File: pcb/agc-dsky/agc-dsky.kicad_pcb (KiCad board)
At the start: 2 copper layers, 100 x 100 mm, 130 parts, among them IC1 TPS62132, IC10 LDS-3161AX, IC11 LDS-3161AX, IC12 LDS-3161AX, IC13 LDS-3161AX, IC14 LDS-3161AX, IC15 LDS-3161AX, IC16 LDS-3161AX, IC17 LDS-3161AX, IC18 LDS-3161AX, IC19 LDS-3161AX, IC2 STM32F072RBT6, IC20 LDS-3161AX, IC21 LDS-3161AX, IC22 LDS-3161AX, IC23 LDS-3161AX, IC24 LDS-3161AX, IC25 LDS-3161AX, IC26 LDS-3161AX, IC27 LDS-3161AX, IC3 MCP23S08, IC4 MCP23S08, IC5 MCP23S08, IC6 MCP23S08, IC7 LDS-3161AX, IC8 LDS-3161AX, IC9 LDS-3161AX, J1 MICROUSB, P1 SWD_TC, Q1 FDN327N, Q2 FDN327N, Q3 FDN327N, Q4 FDN327N, Q5 FDN327N, Q6 FDN327N, SW1 SKPMAME010, SW10 SKPMAME010, SW11 SKPMAME010, SW12 SKPMAME010, SW13 SKPMAME010, SW14 SKPMAME010, SW15 SKPMAME010, SW16 SKPMAME010, SW17 SKPMAME010, SW18 SKPMAME010, SW19 SKPMAME010, SW2 SKPMAME010, SW20 SKPMAME010, SW3 SKPMAME010, SW4 SKPMAME010, SW5 SKPMAME010, SW6 SKPMAME010, SW7 SKPMAME010, SW8 SKPMAME010, SW9 SKHHALA010

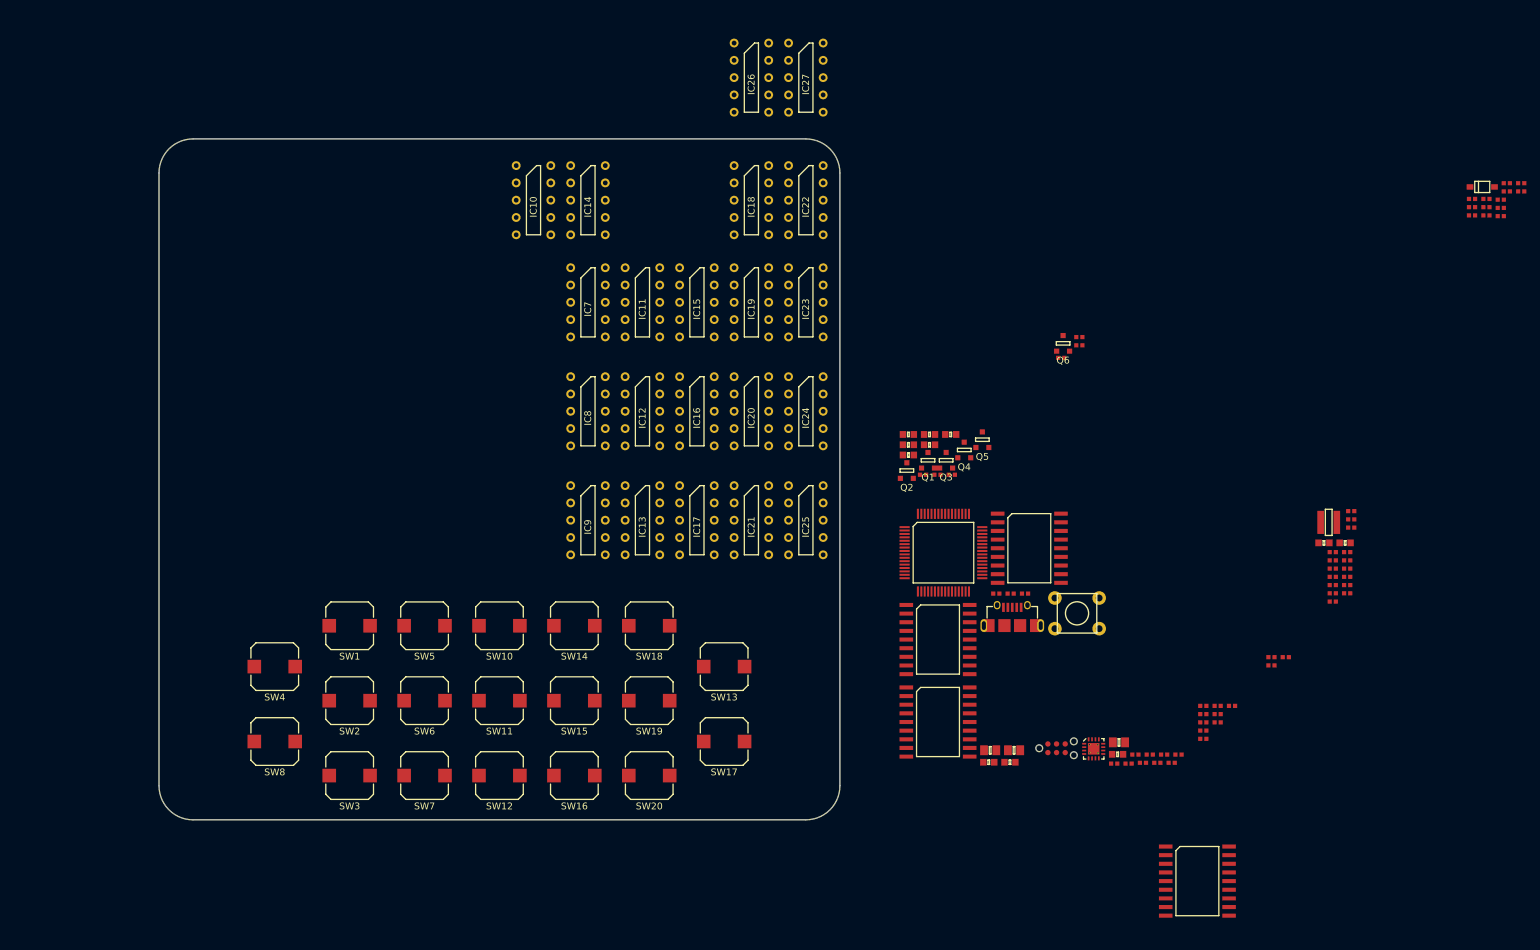
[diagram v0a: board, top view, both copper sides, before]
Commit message: Progress with DSKY board layout
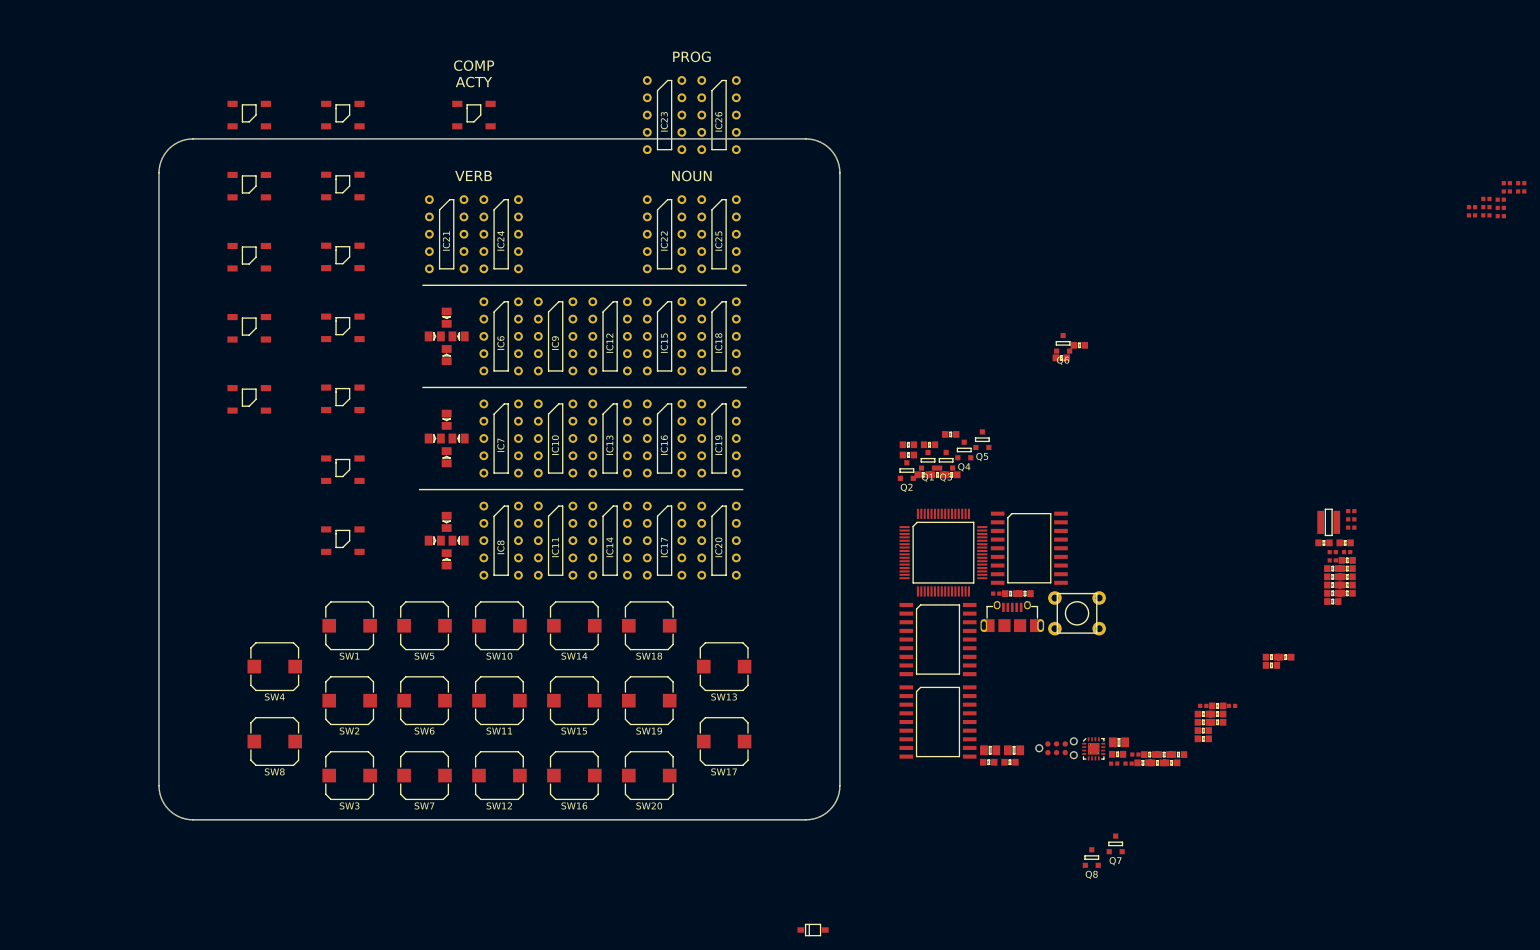
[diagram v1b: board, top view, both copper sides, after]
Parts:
- removed C31: 100nF, agg:0402
- removed R40, R42: 1M, agg:0603
- removed R41: 120, agg:0402
- added D10: LED, agg:0805-LED, F.Cu at (120.5, 74.0)
- added D11: LED, agg:0805-LED, F.Cu at (120.5, 89.0)
- added D12: LED, agg:0805-LED, F.Cu at (120.5, 104.0)
- added D13: MMSD4148T1G, agg:SOD-123, F.Cu at (176.1, 161.2)
- added D2: LED, agg:0805-LED, F.Cu at (122.2, 86.2)
- added D3: LED, agg:0805-LED, F.Cu at (122.2, 101.2)
- added D4: LED, agg:0805-LED, F.Cu at (124.0, 74.0)
- added D5: LED, agg:0805-LED, F.Cu at (124.0, 89.0)
- added D6: LED, agg:0805-LED, F.Cu at (124.0, 104.0)
- added D7: LED, agg:0805-LED, F.Cu at (122.2, 76.8)
- added D8: LED, agg:0805-LED, F.Cu at (122.2, 91.8)
- added D9: LED, agg:0805-LED, F.Cu at (122.2, 106.8)
- added IC28: WS2812B, agc-dsky:WS2812B, F.Cu at (93.2, 41.5)
- added IC29: WS2812B, agc-dsky:WS2812B, F.Cu at (93.2, 51.9)
- added IC30: WS2812B, agc-dsky:WS2812B, F.Cu at (93.2, 62.4)
- added IC31: WS2812B, agc-dsky:WS2812B, F.Cu at (93.2, 72.8)
- added IC32: WS2812B, agc-dsky:WS2812B, F.Cu at (93.2, 83.2)
- added IC33: WS2812B, agc-dsky:WS2812B, F.Cu at (107.0, 41.5)
- added IC34: WS2812B, agc-dsky:WS2812B, F.Cu at (107.0, 51.9)
- added IC35: WS2812B, agc-dsky:WS2812B, F.Cu at (107.0, 62.3)
- added IC36: WS2812B, agc-dsky:WS2812B, F.Cu at (107.0, 72.7)
- added IC37: WS2812B, agc-dsky:WS2812B, F.Cu at (107.0, 83.2)
- added IC38: WS2812B, agc-dsky:WS2812B, F.Cu at (107.0, 93.6)
- added IC39: WS2812B, agc-dsky:WS2812B, F.Cu at (107.0, 104.0)
- added Q7: FDN327N, agc-dsky:supersot-3, F.Cu at (220.5, 148.5)
- added Q8: FDN327N, agc-dsky:supersot-3, F.Cu at (217.0, 150.5)
- D1: value MMSD4148T1G -> LED; footprint agg:SOD-123 -> agg:0805-LED
- IC27: value LDS-3161AX -> WS2812B; footprint agc-dsky:LDS-3161AX -> agc-dsky:WS2812B
- IC6: value MCP23S08 -> LDS-3161AX; footprint agc-dsky:SOIC-18-W -> agc-dsky:LDS-3161AX
- R10, R11, R12, R13, R14, R15, R16, R17, R18, R19, R20, R21, R22, R23, R24, R26, R28, R3, R30, R4, R5, R6, R7, R8, R9: value 120 -> 100; footprint agg:0402 -> agg:0603
- R25, R27, R29, R31, R33, R35, R37, R39: value 120 -> 1M; footprint agg:0402 -> agg:0603
- R32, R34, R36, R38: value 1M -> 100
- moved D1 153.3 mm to (122.2, 71.2), turned to 90 degrees
- moved IC6 129.8 mm to (130.2, 74.0)
- moved IC21 61.4 mm to (122.2, 59.0)
- moved IC24 51.8 mm to (130.2, 59.0)
- moved IC14 50.1 mm to (146.2, 104.0)
- moved IC27 49.1 mm to (126.2, 41.5)
- moved IC25 43.9 mm to (162.2, 59.0)
- moved IC11 37.2 mm to (138.2, 104.0)
- moved IC10 35.2 mm to (138.2, 89.0)
- moved IC23 34.5 mm to (154.2, 41.5)
- moved IC9 27.4 mm to (138.2, 74.0)
- moved IC7 23.7 mm to (130.2, 89.0)
- moved IC8 22.9 mm to (130.2, 104.0)
- moved IC22 21.3 mm to (154.2, 59.0)
- moved IC18 20.6 mm to (162.2, 74.0)
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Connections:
- C18 pad 1: 3v3 -> 5v
- C19 pad 1: Net-(C19-Pad1) -> 5v
- C23 pad 1: 5v -> Net-(C23-Pad1)
- D1 pad 1: Net-(C19-Pad1) -> Net-(D1-Pad1)
- D1 pad 2: 5v -> /7-segs/D1
- IC10 pad 10: /7-segs/A4 -> /7-segs/A2
- IC10 pad 2: /7-segs/F4 -> /7-segs/F2
- IC10 pad 3: /7-segs/G4 -> /7-segs/G2
- IC10 pad 4: /7-segs/E4 -> /7-segs/E2
- IC10 pad 5: /7-segs/D4 -> /7-segs/D2
- IC10 pad 8: /7-segs/C4 -> /7-segs/C2
- IC10 pad 9: /7-segs/B4 -> /7-segs/B2
- IC11 pad 1: Net-(IC11-Pad1) -> Net-(IC10-Pad1)
- IC11 pad 10: /7-segs/A1 -> /7-segs/A3
- IC11 pad 2: /7-segs/F1 -> /7-segs/F3
- IC11 pad 3: /7-segs/G1 -> /7-segs/G3
- IC11 pad 4: /7-segs/E1 -> /7-segs/E3
- IC11 pad 5: /7-segs/D1 -> /7-segs/D3
- IC11 pad 6: Net-(IC11-Pad1) -> Net-(IC10-Pad1)
- IC11 pad 8: /7-segs/C1 -> /7-segs/C3
- IC11 pad 9: /7-segs/B1 -> /7-segs/B3
- IC12 pad 1: Net-(IC11-Pad1) -> Net-(IC12-Pad1)
- IC12 pad 10: /7-segs/A2 -> /7-segs/A1
- IC12 pad 2: /7-segs/F2 -> /7-segs/F1
- IC12 pad 3: /7-segs/G2 -> /7-segs/G1
- IC12 pad 4: /7-segs/E2 -> /7-segs/E1
- IC12 pad 5: /7-segs/D2 -> /7-segs/D1
- IC12 pad 6: Net-(IC11-Pad1) -> Net-(IC12-Pad1)
- IC12 pad 8: /7-segs/C2 -> /7-segs/C1
- IC12 pad 9: /7-segs/B2 -> /7-segs/B1
- IC13 pad 1: Net-(IC11-Pad1) -> Net-(IC12-Pad1)
- IC13 pad 10: /7-segs/A3 -> /7-segs/A2
- IC13 pad 2: /7-segs/F3 -> /7-segs/F2
- IC13 pad 3: /7-segs/G3 -> /7-segs/G2
- IC13 pad 4: /7-segs/E3 -> /7-segs/E2
- IC13 pad 5: /7-segs/D3 -> /7-segs/D2
- IC13 pad 6: Net-(IC11-Pad1) -> Net-(IC12-Pad1)
- IC13 pad 8: /7-segs/C3 -> /7-segs/C2
- IC13 pad 9: /7-segs/B3 -> /7-segs/B2
- IC14 pad 1: Net-(IC11-Pad1) -> Net-(IC12-Pad1)
- IC14 pad 10: /7-segs/A4 -> /7-segs/A3
- IC14 pad 2: /7-segs/F4 -> /7-segs/F3
- IC14 pad 3: /7-segs/G4 -> /7-segs/G3
- IC14 pad 4: /7-segs/E4 -> /7-segs/E3
- IC14 pad 5: /7-segs/D4 -> /7-segs/D3
- IC14 pad 6: Net-(IC11-Pad1) -> Net-(IC12-Pad1)
- IC14 pad 8: /7-segs/C4 -> /7-segs/C3
- IC14 pad 9: /7-segs/B4 -> /7-segs/B3
- IC18 pad 1: Net-(IC15-Pad1) -> Net-(IC18-Pad1)
- IC18 pad 10: /7-segs/A4 -> /7-segs/A1
- IC18 pad 2: /7-segs/F4 -> /7-segs/F1
- IC18 pad 3: /7-segs/G4 -> /7-segs/G1
- IC18 pad 4: /7-segs/E4 -> /7-segs/E1
- IC18 pad 5: /7-segs/D4 -> /7-segs/D1
- IC18 pad 6: Net-(IC15-Pad1) -> Net-(IC18-Pad1)
- IC18 pad 8: /7-segs/C4 -> /7-segs/C1
- IC18 pad 9: /7-segs/B4 -> /7-segs/B1
- IC19 pad 1: Net-(IC19-Pad1) -> Net-(IC18-Pad1)
- IC19 pad 10: /7-segs/A1 -> /7-segs/A2
- IC19 pad 2: /7-segs/F1 -> /7-segs/F2
- IC19 pad 3: /7-segs/G1 -> /7-segs/G2
- IC19 pad 4: /7-segs/E1 -> /7-segs/E2
- IC19 pad 5: /7-segs/D1 -> /7-segs/D2
- IC19 pad 6: Net-(IC19-Pad1) -> Net-(IC18-Pad1)
- IC19 pad 8: /7-segs/C1 -> /7-segs/C2
- IC19 pad 9: /7-segs/B1 -> /7-segs/B2
- IC2 pad 10: Net-(IC2-Pad10) -> (no net)
- IC2 pad 11: Net-(IC2-Pad11) -> (no net)
- IC2 pad 14: Net-(IC2-Pad14) -> (no net)
- IC2 pad 15: Net-(IC2-Pad15) -> (no net)
- IC2 pad 16: Net-(IC2-Pad16) -> (no net)
- IC2 pad 17: Net-(IC2-Pad17) -> (no net)
- IC2 pad 20: Net-(IC2-Pad20) -> (no net)
- IC2 pad 28: Net-(IC2-Pad28) -> (no net)
- IC2 pad 29: Net-(IC2-Pad29) -> /Co8
- IC2 pad 3: Net-(IC2-Pad3) -> (no net)
- IC2 pad 37: /NRST_4 -> (no net)
- IC2 pad 38: /NCS_4 -> (no net)
- IC2 pad 4: Net-(IC2-Pad4) -> (no net)
- IC2 pad 5: Net-(IC2-Pad5) -> (no net)
- IC2 pad 50: Net-(IC2-Pad50) -> (no net)
- IC2 pad 51: Net-(IC2-Pad51) -> (no net)
- IC2 pad 52: Net-(IC2-Pad52) -> (no net)
- IC2 pad 53: Net-(IC2-Pad53) -> (no net)
- IC2 pad 54: Net-(IC2-Pad54) -> (no net)
- IC2 pad 6: Net-(IC2-Pad6) -> (no net)
- IC2 pad 62: Net-(IC2-Pad62) -> /Co7
- IC2 pad 8: Net-(IC2-Pad8) -> (no net)
- IC2 pad 9: Net-(IC2-Pad9) -> (no net)
- IC20 pad 1: Net-(IC19-Pad1) -> Net-(IC18-Pad1)
- IC20 pad 10: /7-segs/A2 -> /7-segs/A3
- IC20 pad 2: /7-segs/F2 -> /7-segs/F3
- IC20 pad 3: /7-segs/G2 -> /7-segs/G3
- IC20 pad 4: /7-segs/E2 -> /7-segs/E3
- IC20 pad 5: /7-segs/D2 -> /7-segs/D3
- IC20 pad 6: Net-(IC19-Pad1) -> Net-(IC18-Pad1)
- IC20 pad 8: /7-segs/C2 -> /7-segs/C3
- IC20 pad 9: /7-segs/B2 -> /7-segs/B3
- IC21 pad 1: Net-(IC19-Pad1) -> Net-(IC21-Pad1)
- IC21 pad 10: /7-segs/A3 -> /7-segs/A1
- IC21 pad 2: /7-segs/F3 -> /7-segs/F1
- IC21 pad 3: /7-segs/G3 -> /7-segs/G1
- IC21 pad 4: /7-segs/E3 -> /7-segs/E1
- IC21 pad 5: /7-segs/D3 -> /7-segs/D1
- IC21 pad 6: Net-(IC19-Pad1) -> Net-(IC21-Pad1)
- IC21 pad 8: /7-segs/C3 -> /7-segs/C1
- IC21 pad 9: /7-segs/B3 -> /7-segs/B1
- IC22 pad 1: Net-(IC19-Pad1) -> Net-(IC21-Pad1)
- IC22 pad 10: /7-segs/A4 -> /7-segs/A2
- IC22 pad 2: /7-segs/F4 -> /7-segs/F2
- IC22 pad 3: /7-segs/G4 -> /7-segs/G2
- IC22 pad 4: /7-segs/E4 -> /7-segs/E2
- IC22 pad 5: /7-segs/D4 -> /7-segs/D2
- IC22 pad 6: Net-(IC19-Pad1) -> Net-(IC21-Pad1)
- IC22 pad 8: /7-segs/C4 -> /7-segs/C2
- IC22 pad 9: /7-segs/B4 -> /7-segs/B2
- IC23 pad 1: Net-(IC23-Pad1) -> Net-(IC21-Pad1)
- IC23 pad 10: /7-segs/A1 -> /7-segs/A3
- IC23 pad 2: /7-segs/F1 -> /7-segs/F3
- IC23 pad 3: /7-segs/G1 -> /7-segs/G3
- IC23 pad 4: /7-segs/E1 -> /7-segs/E3
- IC23 pad 5: /7-segs/D1 -> /7-segs/D3
- IC23 pad 6: Net-(IC23-Pad1) -> Net-(IC21-Pad1)
- IC23 pad 8: /7-segs/C1 -> /7-segs/C3
- IC23 pad 9: /7-segs/B1 -> /7-segs/B3
- IC24 pad 1: Net-(IC23-Pad1) -> Net-(IC24-Pad1)
- IC24 pad 10: /7-segs/A2 -> /7-segs/A1
- IC24 pad 2: /7-segs/F2 -> /7-segs/F1
- IC24 pad 3: /7-segs/G2 -> /7-segs/G1
- IC24 pad 4: /7-segs/E2 -> /7-segs/E1
- IC24 pad 5: /7-segs/D2 -> /7-segs/D1
- IC24 pad 6: Net-(IC23-Pad1) -> Net-(IC24-Pad1)
- IC24 pad 8: /7-segs/C2 -> /7-segs/C1
- IC24 pad 9: /7-segs/B2 -> /7-segs/B1
- IC25 pad 1: Net-(IC23-Pad1) -> Net-(IC24-Pad1)
- IC25 pad 10: /7-segs/A3 -> /7-segs/A2
- IC25 pad 2: /7-segs/F3 -> /7-segs/F2
- IC25 pad 3: /7-segs/G3 -> /7-segs/G2
- IC25 pad 4: /7-segs/E3 -> /7-segs/E2
- IC25 pad 5: /7-segs/D3 -> /7-segs/D2
- IC25 pad 6: Net-(IC23-Pad1) -> Net-(IC24-Pad1)
- IC25 pad 8: /7-segs/C3 -> /7-segs/C2
- IC25 pad 9: /7-segs/B3 -> /7-segs/B2
- IC26 pad 1: Net-(IC23-Pad1) -> Net-(IC24-Pad1)
- IC26 pad 10: /7-segs/A4 -> /7-segs/A3
- IC26 pad 2: /7-segs/F4 -> /7-segs/F3
- IC26 pad 3: /7-segs/G4 -> /7-segs/G3
- IC26 pad 4: /7-segs/E4 -> /7-segs/E3
- IC26 pad 5: /7-segs/D4 -> /7-segs/D3
- IC26 pad 6: Net-(IC23-Pad1) -> Net-(IC24-Pad1)
- IC26 pad 8: /7-segs/C4 -> /7-segs/C3
- IC26 pad 9: /7-segs/B4 -> /7-segs/B3
- IC27 pad 1: Net-(IC27-Pad1) -> Net-(C23-Pad1)
- IC27 pad 2: /7-segs/F4 -> Net-(IC27-Pad2)
- IC27 pad 3: /7-segs/G4 -> GND
- IC27 pad 4: /7-segs/E4 -> /LED_DIN
- IC3 pad 17: Net-(IC3-Pad17) -> (no net)
- IC3 pad 8: Net-(IC3-Pad8) -> (no net)
- IC4 pad 17: Net-(IC4-Pad17) -> (no net)
- IC4 pad 8: Net-(IC4-Pad8) -> (no net)
- IC5 pad 17: Net-(IC5-Pad17) -> (no net)
- IC5 pad 5: GND -> 3v3
- IC5 pad 8: Net-(IC5-Pad8) -> (no net)
- IC6 pad 1: /SPI2_SCK -> Net-(IC6-Pad1)
- IC6 pad 10: Net-(IC6-Pad10) -> /7-segs/A1
- IC6 pad 2: /SPI2_SI -> /7-segs/F1
- IC6 pad 3: /SPI2_SO -> /7-segs/G1
- IC6 pad 4: 3v3 -> /7-segs/E1
- IC6 pad 5: 3v3 -> /7-segs/D1
- IC6 pad 6: /NRST_4 -> Net-(IC6-Pad1)
- IC6 pad 7: /NCS_4 -> GND
- IC6 pad 8: Net-(IC6-Pad8) -> /7-segs/C1
- IC6 pad 9: GND -> /7-segs/B1
- IC7 pad 1: Net-(IC10-Pad1) -> Net-(IC6-Pad1)
- IC7 pad 10: /7-segs/A1 -> /7-segs/A2
- IC7 pad 2: /7-segs/F1 -> /7-segs/F2
- IC7 pad 3: /7-segs/G1 -> /7-segs/G2
- IC7 pad 4: /7-segs/E1 -> /7-segs/E2
- IC7 pad 5: /7-segs/D1 -> /7-segs/D2
- IC7 pad 6: Net-(IC10-Pad1) -> Net-(IC6-Pad1)
- IC7 pad 8: /7-segs/C1 -> /7-segs/C2
- IC7 pad 9: /7-segs/B1 -> /7-segs/B2
- IC8 pad 1: Net-(IC10-Pad1) -> Net-(IC6-Pad1)
- IC8 pad 10: /7-segs/A2 -> /7-segs/A3
- IC8 pad 2: /7-segs/F2 -> /7-segs/F3
- IC8 pad 3: /7-segs/G2 -> /7-segs/G3
- IC8 pad 4: /7-segs/E2 -> /7-segs/E3
- IC8 pad 5: /7-segs/D2 -> /7-segs/D3
- IC8 pad 6: Net-(IC10-Pad1) -> Net-(IC6-Pad1)
- IC8 pad 8: /7-segs/C2 -> /7-segs/C3
- IC8 pad 9: /7-segs/B2 -> /7-segs/B3
- IC9 pad 10: /7-segs/A3 -> /7-segs/A1
- IC9 pad 2: /7-segs/F3 -> /7-segs/F1
- IC9 pad 3: /7-segs/G3 -> /7-segs/G1
- IC9 pad 4: /7-segs/E3 -> /7-segs/E1
- IC9 pad 5: /7-segs/D3 -> /7-segs/D1
- IC9 pad 8: /7-segs/C3 -> /7-segs/C1
- IC9 pad 9: /7-segs/B3 -> /7-segs/B1
- J1 pad 4: Net-(J1-Pad4) -> (no net)
- J1 pad S: Net-(J1-PadS) -> (no net)
- P1 pad 6: Net-(P1-Pad6) -> (no net)
- Q1 pad D: Net-(IC10-Pad1) -> Net-(IC6-Pad1)
- Q2 pad D: Net-(IC11-Pad1) -> Net-(IC10-Pad1)
- Q3 pad D: Net-(IC15-Pad1) -> Net-(IC12-Pad1)
- Q4 pad D: Net-(IC19-Pad1) -> Net-(IC15-Pad1)
- Q5 pad D: Net-(IC23-Pad1) -> Net-(IC18-Pad1)
- Q6 pad D: Net-(IC27-Pad1) -> Net-(IC21-Pad1)
- R10 pad 1: /7-segs/F4 -> Net-(IC3-Pad14)
- R10 pad 2: Net-(IC6-Pad15) -> /7-segs/E1
- R11 pad 1: /7-segs/B1 -> Net-(IC4-Pad11)
- R11 pad 2: Net-(IC3-Pad11) -> /7-segs/B2
- R12 pad 1: /7-segs/E1 -> Net-(IC4-Pad14)
- R12 pad 2: Net-(IC3-Pad14) -> /7-segs/E2
- R13 pad 1: /7-segs/B2 -> Net-(IC5-Pad11)
- R13 pad 2: Net-(IC4-Pad11) -> /7-segs/B3
- R14 pad 1: /7-segs/E2 -> Net-(IC5-Pad14)
- R14 pad 2: Net-(IC4-Pad14) -> /7-segs/E3
- R15 pad 1: /7-segs/B3 -> Net-(IC3-Pad10)
- R15 pad 2: Net-(IC5-Pad11) -> /7-segs/A1
- R16 pad 1: /7-segs/E3 -> Net-(IC3-Pad13)
- R16 pad 2: Net-(IC5-Pad14) -> /7-segs/D1
- R17 pad 1: /7-segs/B4 -> Net-(IC3-Pad16)
- R17 pad 2: Net-(IC6-Pad11) -> /7-segs/G1
- R18 pad 1: /7-segs/E4 -> Net-(IC4-Pad10)
- R18 pad 2: Net-(IC6-Pad14) -> /7-segs/A2
- R19 pad 1: /7-segs/A1 -> Net-(IC4-Pad13)
- R19 pad 2: Net-(IC3-Pad10) -> /7-segs/D2
- R20 pad 1: /7-segs/D1 -> Net-(IC4-Pad16)
- R20 pad 2: Net-(IC3-Pad13) -> /7-segs/G2
- R21 pad 1: /7-segs/G1 -> Net-(IC5-Pad10)
- R21 pad 2: Net-(IC3-Pad16) -> /7-segs/A3
- R22 pad 1: /7-segs/A2 -> Net-(IC5-Pad13)
- R22 pad 2: Net-(IC4-Pad10) -> /7-segs/D3
- R23 pad 1: /7-segs/D2 -> Net-(IC5-Pad16)
- R23 pad 2: Net-(IC4-Pad13) -> /7-segs/G3
- R24 pad 1: /7-segs/G2 -> /Co1
- R24 pad 2: Net-(IC4-Pad16) -> Net-(Q1-PadG)
- R25 pad 1: /7-segs/A3 -> Net-(Q1-PadG)
- R25 pad 2: Net-(IC5-Pad10) -> GND
- R26 pad 1: /7-segs/D3 -> /Co2
- R26 pad 2: Net-(IC5-Pad13) -> Net-(Q2-PadG)
- R27 pad 1: /7-segs/G3 -> Net-(Q2-PadG)
- R27 pad 2: Net-(IC5-Pad16) -> GND
- R28 pad 1: /7-segs/A4 -> /Co3
- R28 pad 2: Net-(IC6-Pad10) -> Net-(Q3-PadG)
- R29 pad 1: /7-segs/D4 -> Net-(Q3-PadG)
- R29 pad 2: Net-(IC6-Pad13) -> GND
- R3 pad 1: /7-segs/C1 -> Net-(IC3-Pad12)
- R3 pad 2: Net-(IC3-Pad12) -> /7-segs/C1
- R30 pad 1: /7-segs/G4 -> /Co4
- R30 pad 2: Net-(IC6-Pad16) -> Net-(Q4-PadG)
- R31 pad 1: /Co1 -> Net-(Q4-PadG)
- R31 pad 2: Net-(Q1-PadG) -> GND
- R32 pad 1: Net-(Q1-PadG) -> /Co5
- R32 pad 2: GND -> Net-(Q5-PadG)
- R33 pad 1: /Co2 -> Net-(Q5-PadG)
- R33 pad 2: Net-(Q2-PadG) -> GND
- R34 pad 1: Net-(Q2-PadG) -> /Co6
- R34 pad 2: GND -> Net-(Q6-PadG)
- R35 pad 1: /Co3 -> Net-(Q6-PadG)
- R35 pad 2: Net-(Q3-PadG) -> GND
- R36 pad 1: Net-(Q3-PadG) -> /Co7
- R36 pad 2: GND -> Net-(Q7-PadG)
- R37 pad 1: /Co4 -> Net-(Q7-PadG)
- R37 pad 2: Net-(Q4-PadG) -> GND
- R38 pad 1: Net-(Q4-PadG) -> /Co8
- R38 pad 2: GND -> Net-(Q8-PadG)
- R39 pad 1: /Co5 -> Net-(Q8-PadG)
- R39 pad 2: Net-(Q5-PadG) -> GND
- R4 pad 1: /7-segs/F1 -> Net-(IC3-Pad15)
- R4 pad 2: Net-(IC3-Pad15) -> /7-segs/F1
- R5 pad 1: /7-segs/C2 -> Net-(IC4-Pad12)
- R5 pad 2: Net-(IC4-Pad12) -> /7-segs/C2
- R6 pad 1: /7-segs/F2 -> Net-(IC4-Pad15)
- R6 pad 2: Net-(IC4-Pad15) -> /7-segs/F2
- R7 pad 1: /7-segs/C3 -> Net-(IC5-Pad12)
- R7 pad 2: Net-(IC5-Pad12) -> /7-segs/C3
- R8 pad 1: /7-segs/F3 -> Net-(IC5-Pad15)
- R8 pad 2: Net-(IC5-Pad15) -> /7-segs/F3
- R9 pad 1: /7-segs/C4 -> Net-(IC3-Pad11)
- R9 pad 2: Net-(IC6-Pad12) -> /7-segs/B1
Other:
- rule via_min_drill: 0.3 -> 0.4
- rule via_min_size: 0.4 -> 0.8
- board text added: "COMP ACTY"
- board text added: "PROG"
- board text added: "VERB"

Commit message: Work on routing displays
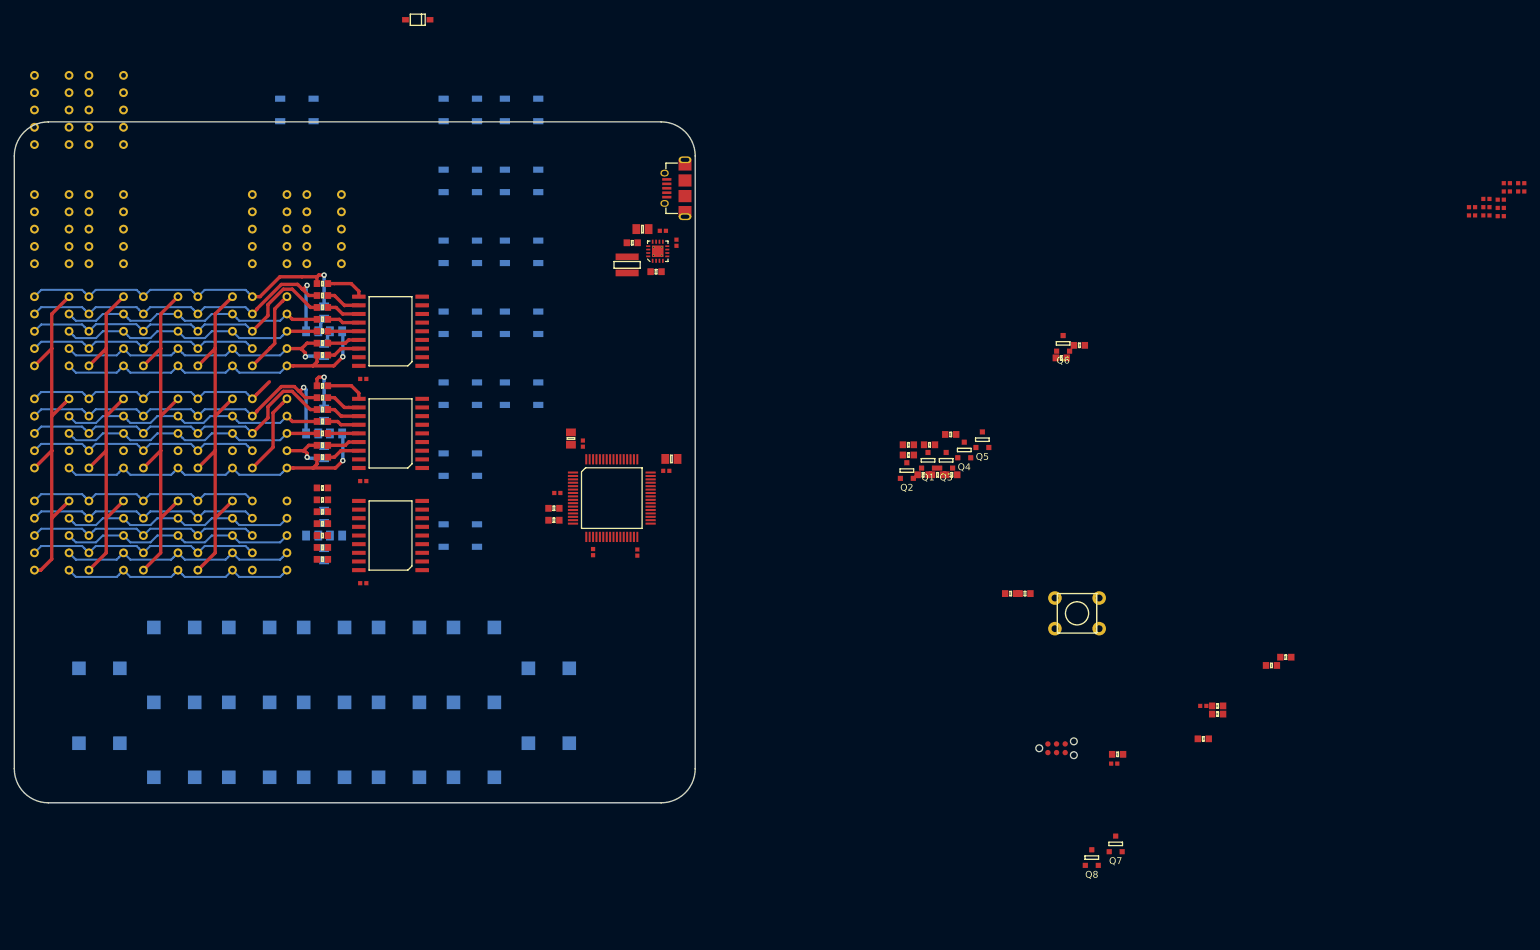
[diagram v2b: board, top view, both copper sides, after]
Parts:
- D1, D10, D11, D12, D2, D3, D4, D5, D6, D7, D8, D9, IC10, IC11, IC12, IC13, IC14, IC15, IC16, IC17, IC18, IC19, IC20, IC21, IC22, IC23, IC24, IC25, IC26, IC27, IC28, IC29, IC30, IC31, IC32, IC33, IC34, IC35, IC36, IC37, IC38, IC39, IC6, IC7, IC8, IC9, SW1, SW10, SW11, SW12, SW13, SW14, SW15, SW16, SW17, SW18, SW19, SW2, SW20, SW3, SW4, SW5, SW6, SW7, SW8: moved to B.Cu
- moved R9 156.4 mm to (104.0, 68.0), turned to 180 degrees
- moved R4 154.9 mm to (104.0, 75.0), turned to 180 degrees
- moved R10 154.2 mm to (104.0, 73.2), turned to 180 degrees
- moved R17 152.2 mm to (104.0, 76.8), turned to 180 degrees
- moved R19 152.0 mm to (104.0, 86.5), turned to 180 degrees
- moved R12 152.0 mm to (104.0, 88.2), turned to 180 degrees
- moved R18 151.0 mm to (104.0, 81.2), turned to 180 degrees
- moved R11 150.5 mm to (104.0, 83.0), turned to 180 degrees
- moved R15 149.8 mm to (104.0, 66.2), turned to 180 degrees
- moved R13 149.0 mm to (104.0, 98.0), turned to 180 degrees
- moved R8 148.6 mm to (104.0, 105.0), turned to 180 degrees
- moved C15 146.7 mm to (110.0, 80.2)
- moved D13 145.7 mm to (118.0, 27.5), turned to 180 degrees
- moved C17 145.5 mm to (110.0, 110.2)
- moved C16 145.2 mm to (110.0, 95.2)
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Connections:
- D1 pad 2: /7-segs/D1 -> /7-segs/E1
- D2 pad 2: /7-segs/D2 -> /7-segs/E2
- D3 pad 2: /7-segs/D3 -> /7-segs/E3
- D4 pad 2: /7-segs/C1 -> /7-segs/D1
- D5 pad 2: /7-segs/C2 -> /7-segs/D2
- D6 pad 2: /7-segs/C3 -> /7-segs/D3
- R10 pad 2: /7-segs/E1 -> /7-segs/G1
- R12 pad 2: /7-segs/E2 -> /7-segs/G2
- R14 pad 2: /7-segs/E3 -> /7-segs/G3
- R16 pad 2: /7-segs/D1 -> /7-segs/F1
- R17 pad 2: /7-segs/G1 -> /7-segs/D1
- R19 pad 2: /7-segs/D2 -> /7-segs/F2
- R20 pad 2: /7-segs/G2 -> /7-segs/D2
- R22 pad 2: /7-segs/D3 -> /7-segs/F3
- R23 pad 2: /7-segs/G3 -> /7-segs/D3
- R4 pad 2: /7-segs/F1 -> /7-segs/E1
- R6 pad 2: /7-segs/F2 -> /7-segs/E2
- R8 pad 2: /7-segs/F3 -> /7-segs/E3
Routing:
- net GND: track 0.00 -> 105.9 mm
- net Net-(IC18-Pad1): track 0.00 -> 57.2 mm
- net Net-(IC15-Pad1): track 0.00 -> 56.6 mm
- net Net-(IC12-Pad1): track 0.00 -> 56.6 mm
- net Net-(IC10-Pad1): track 0.00 -> 56.6 mm
- net /7-segs/B2: track 0.00 -> 55.2 mm, vias 0 -> 1
- net /7-segs/B1: track 0.00 -> 55.1 mm, vias 0 -> 1
- net /7-segs/A1: track 0.00 -> 52.8 mm, vias 0 -> 1
- net /7-segs/D2: track 0.00 -> 49.8 mm, vias 0 -> 1
- net /7-segs/D1: track 0.00 -> 49.7 mm, vias 0 -> 1
- net /7-segs/C1: track 0.00 -> 49.5 mm
- net /7-segs/C2: track 0.00 -> 49.4 mm
- net /7-segs/A2: track 0.00 -> 45.6 mm, vias 0 -> 1
- net /7-segs/E1: track 0.00 -> 44.3 mm, vias 0 -> 1
- net /7-segs/F2: track 0.00 -> 40.1 mm
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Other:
- net class Power added: clearance 0.2, trace_width 0.5, via_dia 0.8, via_drill 0.4
- board text added: "ALT"
- board text added: "GIMBAL LOCK"
- board text added: "KEY REL"
- board text added: "NO ATT"
- board text added: "OPR ERR"
- board text added: "RESTART"
- board text added: "STBY"
- board text added: "TEMP"
- board text added: "TRACKER"
- board text added: "UPLINK ACTY"
- board text added: "VEL"

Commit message: More work on routing displays
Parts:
- moved Q7 169.5 mm to (88.0, 42.8)
- moved IC21 36.4 mm to (72.2, 40.8)
- moved IC24 36.4 mm to (64.2, 40.8)
- moved IC22 32.0 mm to (104.2, 58.2)
- moved IC25 32.0 mm to (96.2, 58.2)
- moved IC23 17.5 mm to (72.2, 58.2)
- moved IC26 17.5 mm to (64.2, 58.2)
- moved D3 5.51 mm to (104.0, 106.0), turned to 270 degrees
- moved D12 3.40 mm to (104.0, 100.5), turned to 90 degrees
- moved D9 3.40 mm to (102.2, 103.2), turned to 180 degrees
- moved D6 3.25 mm to (105.8, 103.2), turned to 0 degrees
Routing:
- net Net-(IC24-Pad1): track 0.00 -> 88.1 mm
- net /7-segs/E2: track 8.65 -> 91.9 mm, vias 1 -> 2
- net /7-segs/B3: track 35.3 -> 113.8 mm, vias 0 -> 1
- net GND: track 105.9 -> 181.9 mm
- net /7-segs/A3: track 35.3 -> 110.9 mm, vias 0 -> 1
- net /7-segs/C3: track 35.3 -> 108.8 mm
- net /7-segs/D3: track 35.3 -> 104.7 mm, vias 0 -> 1
- net /7-segs/E3: track 35.3 -> 101.8 mm, vias 0 -> 1
- net /7-segs/F3: track 35.3 -> 98.4 mm
- net /7-segs/G3: track 35.3 -> 98.0 mm
- net /7-segs/B1: track 55.1 -> 110.8 mm
- net /7-segs/A1: track 52.8 -> 108.5 mm
- net /7-segs/A2: track 45.6 -> 97.8 mm
- net Net-(IC21-Pad1): track 0.00 -> 51.9 mm
- net /7-segs/C1: track 49.5 -> 99.9 mm
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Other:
- board size 100 x 100 mm -> 100 x 115 mm
